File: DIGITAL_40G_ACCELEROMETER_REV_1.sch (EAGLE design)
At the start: 22 parts, among them IC1 ADIS16500AMLZ, IC2 LTC6820IUD#PBF, IC3 LDL1117S33R, T1 782482_33VC

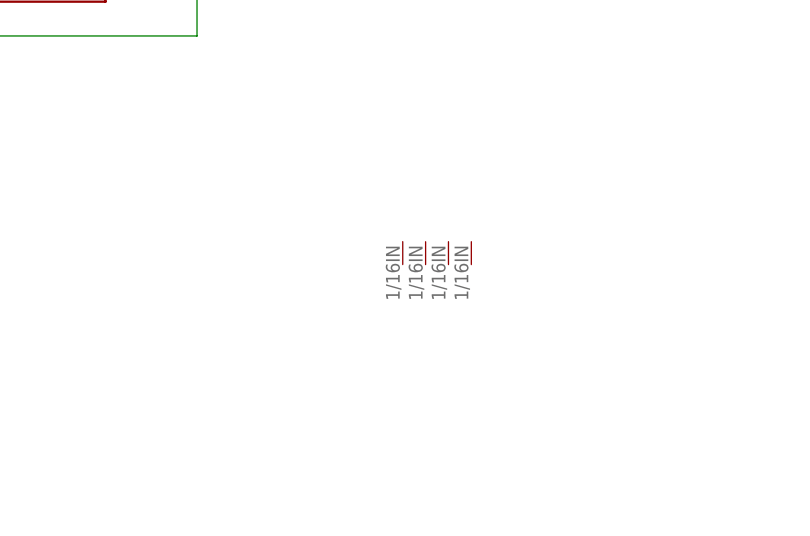
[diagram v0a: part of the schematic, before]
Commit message: Final final preliminary board layout update. Back to 2 screw holes and sized at 1.25 inches square.
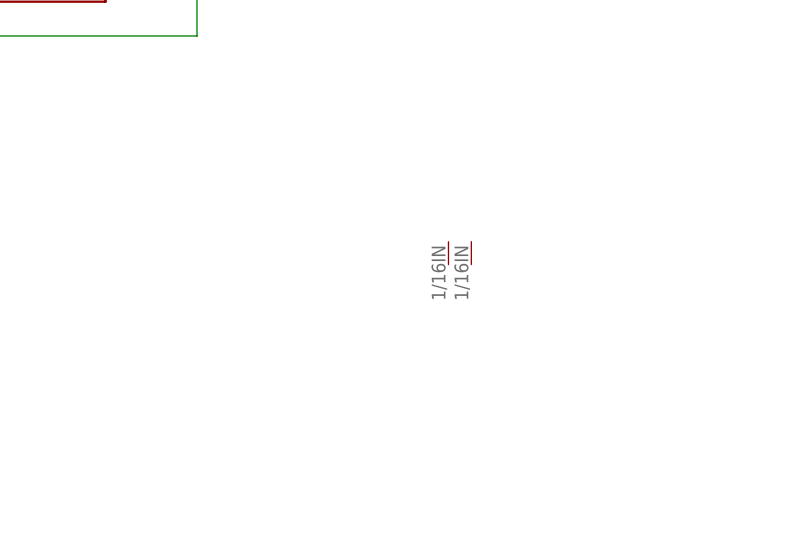
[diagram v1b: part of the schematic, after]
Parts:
- removed U$1, U$2: THROUGH_HOLE, SamacSys_Parts:THROUGH_HOLE
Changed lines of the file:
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@@
 <part name="GND20" library="supply1" library_urn="urn:adsk.eagle:library:371" deviceset="GND" device=""/>
 <part name="GND21" library="supply1" library_urn="urn:adsk.eagle:library:371" deviceset="GND" device=""/>
-<part name="U$1" library="SamacSys_Parts" library_urn="urn:adsk.eagle:library:31941355" deviceset="THROUGH_HOLE" device="" package3d_urn="urn:adsk.eagle:package:35094096/3"/>
-<part name="U$2" library="SamacSys_Parts" library_urn="urn:adsk.eagle:library:31941355" deviceset="THROUGH_HOLE" device="" package3d_urn="urn:adsk.eagle:package:35094096/3"/>
 <part name="U$3" library="SamacSys_Parts" library_urn="urn:adsk.eagle:library:31941355" deviceset="THROUGH_HOLE" device="" package3d_urn="urn:adsk.eagle:package:35094096/3"/>
 <part name="U$4" library="SamacSys_Parts" library_urn="urn:adsk.eagle:library:31941355" deviceset="THROUGH_HOLE" device="" package3d_urn="urn:adsk.eagle:package:35094096/3"/>
@@
 <attribute name="VALUE" x="373.38" y="45.72" size="1.778" layer="96" rot="R90"/>
 </instance>
-<instance part="U$1" gate="G$1" x="162.56" y="-10.16" smashed="yes"/>
-<instance part="U$2" gate="G$1" x="165.1" y="-10.16" smashed="yes"/>
 <instance part="U$3" gate="G$1" x="167.64" y="-10.16" smashed="yes"/>
 <instance part="U$4" gate="G$1" x="170.18" y="-10.16" smashed="yes"/>
